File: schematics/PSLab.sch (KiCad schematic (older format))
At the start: 76 parts, among them J1 Programmer, J10 GND, J11 Vbus, J13 D+, J14 D-, J15 External Power, J16 I2C-2, J2 DoublePins, J5 Bluetooth, J6 I2C-1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

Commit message: docs: bill of materials
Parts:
- U15: footprint Connector_PinHeader_2.54mm:PinHeader_2x04_P2.54mm_Vertical -> Custom_Components:ESP-01
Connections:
- net +5V: now also J15.1 (Pin_1); no longer J7.1 (Pin_1)
- net ERxD: now also U15.2 (TX); no longer U15.1 (GND)
- net ETxD: now also U15.7 (RX); no longer U15.5 (IO0)
- net ExP: no longer J15.1 (Pin_1)
- net GND: now also U15.1 (GND); no longer U15.8 (VCC)
- net Vdd: now also U15.8 (VCC); no longer U15.2 (TX)
- net IOut: now reaches U3.38 (SCL1/RPI53/RC5)
- net IOut: now also J7.1 (Pin_1)
- no-connect marks 13 -> 12
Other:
- moved on the sheet: C2, R56, R57
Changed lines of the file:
@@
 	-1   0    0    1
 $EndComp
-Text Label 8395 1700 1    60   ~ 0
+Text Label 8910 1710 2    60   ~ 0
 Vdd
 $Comp
 L PSLab-rescue:GND-RESCUE-proto1 #PWR020
 U 1 1 55654875
-P 9170 1175
-F 0 "#PWR020" H 9170 1175 30  0001 C CNN
-F 1 "GND" H 9170 1105 30  0001 C CNN
-F 2 "" H 9170 1175 60  0000 C CNN
-F 3 "" H 9170 1175 60  0000 C CNN
-	1    9170 1175
-	0    -1   -1   0
+P 8470 1175
+F 0 "#PWR020" H 8470 1175 30  0001 C CNN
+F 1 "GND" H 8470 1105 30  0001 C CNN
+F 2 "" H 8470 1175 60  0000 C CNN
+F 3 "" H 8470 1175 60  0000 C CNN
+	1    8470 1175
+	0    1    1    0
 $EndComp
 $Comp
@@
 	0    1    1    0
 $EndComp
-Text Label 9345 1025 1    60   ~ 0
+Text Label 9330 1025 1    60   ~ 0
 ETxD
-Text Label 8395 825  3    60   ~ 0
+Text Label 8395 1040 3    60   ~ 0
 ERxD
 Text GLabel 6085 6665 0    40   Input ~ 0
@@
 L PSLab-rescue:R-RESCUE-proto1 R57
 U 1 1 56654C7F
-P 7775 850
-F 0 "R57" V 7855 850 40  0000 C CNN
-F 1 "18" V 7782 851 40  0000 C CNN
-F 2 "Resistor_SMD:R_0603_1608Metric" V 7705 850 30  0001 C CNN
-F 3 "" H 7775 850 30  0000 C CNN
-	1    7775 850
+P 7760 660
+F 0 "R57" V 7840 660 40  0000 C CNN
+F 1 "18" V 7767 661 40  0000 C CNN
+F 2 "Resistor_SMD:R_0603_1608Metric" V 7690 660 30  0001 C CNN
+F 3 "" H 7760 660 30  0000 C CNN
+	1    7760 660
 	0    1    -1   0
 $EndComp
@@
 L PSLab-rescue:R-RESCUE-proto1 R56
 U 1 1 5665622A
-P 7775 650
-F 0 "R56" V 7855 650 40  0000 C CNN
-F 1 "18" V 7782 651 40  0000 C CNN
-F 2 "Resistor_SMD:R_0603_1608Metric" V 7705 650 30  0001 C CNN
-F 3 "" H 7775 650 30  0000 C CNN
-	1    7775 650
+P 7760 880
+F 0 "R56" V 7840 880 40  0000 C CNN
+F 1 "18" V 7767 881 40  0000 C CNN
+F 2 "Resistor_SMD:R_0603_1608Metric" V 7690 880 30  0001 C CNN
+F 3 "" H 7760 880 30  0000 C CNN
+	1    7760 880
 	0    1    -1   0
 $EndComp
@@
 	-1   0    0    1
 $EndComp
-Text GLabel 7175 1895 1    40   Input ~ 0
-+5V
 Text GLabel 1415 3550 0    40   Input ~ 0
 SQR1
@@
 L PSLab-rescue:GND-RESCUE-proto1 #PWR046
 U 1 1 5564F446
-P 9220 1900
-F 0 "#PWR046" H 9220 1900 30  0001 C CNN
-F 1 "GND" H 9220 1830 30  0001 C CNN
-F 2 "" H 9220 1900 60  0000 C CNN
-F 3 "" H 9220 1900 60  0000 C CNN
-	1    9220 1900
+P 8225 2040
+F 0 "#PWR046" H 8225 2040 30  0001 C CNN
+F 1 "GND" H 8225 1970 30  0001 C CNN
+F 2 "" H 8225 2040 60  0000 C CNN
+F 3 "" H 8225 2040 60  0000 C CNN
+	1    8225 2040
 	1    0    0    -1
 $EndComp
@@
 L PSLab-rescue:C-RESCUE-proto1 C2
 U 1 1 5564F04A
-P 8820 1775
-F 0 "C2" H 8820 1875 40  0000 L CNN
-F 1 "0.1u" H 8826 1690 40  0000 L CNN
-F 2 "Capacitor_SMD:C_0603_1608Metric" H 8858 1625 30  0001 C CNN
-F 3 "" H 8820 1775 60  0000 C CNN
-	1    8820 1775
-	0    -1   -1   0
+P 8225 1840
+F 0 "C2" H 8225 1940 40  0000 L CNN
+F 1 "0.1u" H 8231 1755 40  0000 L CNN
+F 2 "Capacitor_SMD:C_0603_1608Metric" H 8263 1690 30  0001 C CNN
+F 3 "" H 8225 1840 60  0000 C CNN
+	1    8225 1840
+	1    0    0    -1
 $EndComp
 Text GLabel 5450 2300 1    47   Input ~ 0
@@
 Wire Wire Line
 	8195 5520 8370 5520
-Wire Wire Line
-	8200 750  9345 750
-Wire Wire Line
-	8200 750  8200 850
-Wire Wire Line
-	8200 850  8025 850
 Wire Notes Line
 	500  2750 4075 2750
@@
 F 0 "U15" H 9020 1625 39  0000 C CNN
 F 1 "ESP01" H 8670 1625 39  0000 C CNN
-F 2 "Connector_PinHeader_2.54mm:PinHeader_2x04_P2.54mm_Vertical" H 8820 1325 60  0001 C CNN
+F 2 "Custom_Components:ESP-01" H 8820 1325 60  0001 C CNN
 F 3 "" H 8820 1325 60  0001 C CNN
 	1    8820 1325
 	1    0    0    -1
 $EndComp
-Wire Wire Line
-	8470 1475 8395 1475
-Wire Wire Line
-	8470 1275 8395 1275
-Wire Wire Line
-	8395 1275 8395 1475
-Connection ~ 8395 1475
-NoConn ~ 9170 1275
-Wire Wire Line
-	8470 1175 8395 1175
-Wire Wire Line
-	8395 1175 8395 650
-Wire Wire Line
-	9170 1475 9345 1475
-Wire Wire Line
-	9345 1475 9345 750
-Wire Wire Line
-	9220 1900 9220 1775
-Wire Wire Line
-	9220 1775 9020 1775
-Wire Wire Line
-	8620 1775 8395 1775
-Wire Wire Line
-	8395 1475 8395 1775
 $Sheet
 S 1310 1190 550  305
@@
 	1    0    0    -1
 $EndComp
-Wire Wire Line
-	8395 650  8025 650
 Wire Notes Line
 	8040 550  8040 2175
@@
 Wire Notes Line
 	7750 2270 7750 4950
-Text GLabel 10100 1030 2    39   Input ~ 8
-ExP
 $Comp
 L Connector_Generic:Conn_01x05 J7
@@
 	0    1    1    0
 $EndComp
-NoConn ~ 5050 2600
 NoConn ~ 8470 1375
-NoConn ~ 9170 1375
 $Comp
 L PSLab-rescue:R-RESCUE-proto1 R55
@@
 RxD2
 Wire Wire Line
-	6975 650  7525 650
-Wire Wire Line
-	7075 1895 7075 850
-Wire Wire Line
-	7075 850  7525 850
-Wire Wire Line
-	6975 1895 6975 650
+	6975 1895 6975 880
+Wire Wire Line
+	8470 1275 8395 1275
+Wire Wire Line
+	9170 1275 9330 1275
+Wire Wire Line
+	9265 1175 9170 1175
+NoConn ~ 9170 1475
+NoConn ~ 9170 1375
+Wire Wire Line
+	7075 660  7510 660
+Wire Wire Line
+	7075 660  7075 1895
+Wire Wire Line
+	8010 660  9330 660
+Wire Wire Line
+	9330 660  9330 1275
+Wire Wire Line
+	7510 880  6975 880
+Wire Wire Line
+	8010 880  8395 880
+Wire Wire Line
+	8395 880  8395 1275
+Wire Wire Line
+	8225 1475 8395 1475
+Wire Wire Line
+	8395 1475 8395 1710
+Wire Wire Line
+	8395 1710 9265 1710
+Connection ~ 8395 1475
+Wire Wire Line
+	8395 1475 8470 1475
+Wire Wire Line
+	8225 1475 8225 1640
+Wire Wire Line
+	9265 1175 9265 1710
+Text GLabel 5050 2300 1    47   Input ~ 0
+IOut
+Wire Wire Line
+	5050 2300 5050 2600
+Text GLabel 7175 1895 1    47   Input ~ 0
+IOut
+Text GLabel 10100 1030 2    40   Input ~ 0
++5V
 $EndSCHEMATC

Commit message: fix: updated bom with correct footprints
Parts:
- F2: value 2016L100PR(1A) -> 1.5A; footprint Fuse:Fuse_1206_3216Metric -> Fuse:Fuse_1812_4532Metric
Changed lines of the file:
@@
 P 10690 930
 F 0 "F2" V 10517 930 39  0000 C CNN
-F 1 "2016L100PR(1A)" V 10592 930 39  0000 C CNN
-F 2 "Fuse:Fuse_1206_3216Metric" V 10620 930 50  0001 C CNN
-F 3 "https://www.mouser.se/datasheet/2/240/Littelfuse_PTC_2016L_Datasheet.pdf-1372437.pdf" H 10690 930 50  0001 C CNN
+F 1 "1.5A" V 10592 930 39  0000 C CNN
+F 2 "Fuse:Fuse_1812_4532Metric" V 10620 930 50  0001 C CNN
+F 3 "https://www.mouser.fi/datasheet/2/240/Littelfuse_PTC_1812L_Datasheet.pdf-693388.pdf" H 10690 930 50  0001 C CNN
 	1    10690 930
 	0    1    1    0

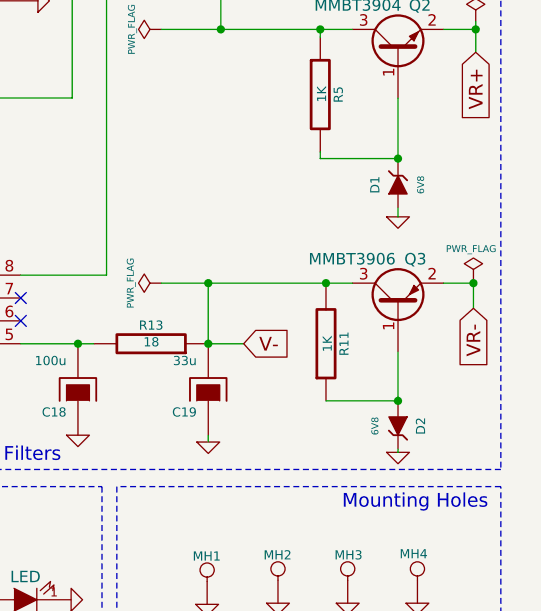
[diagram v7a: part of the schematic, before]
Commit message: fix: position correction for production
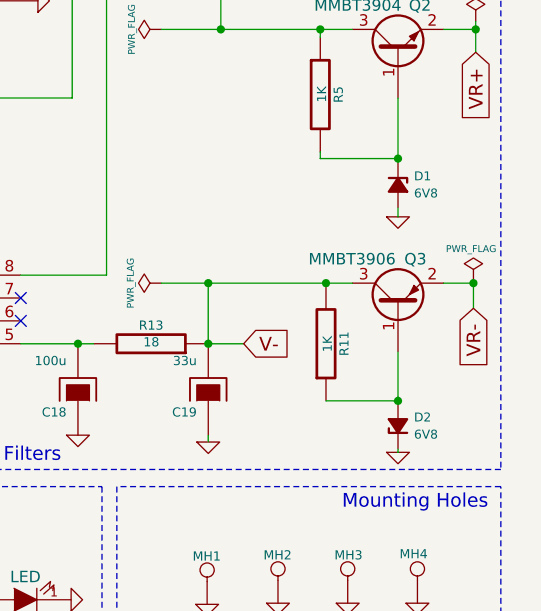
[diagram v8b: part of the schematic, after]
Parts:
- removed D1, D2: 6V8, Diode_SMD:D_MiniMELF, symbol PSLab-rescue:ZENERsmall-RESCUE-proto1
- added D1, D2: 6V8, Diode_SMD:D_MiniMELF, symbol Device:D_Zener_Small_ALT
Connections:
- net GND: now also D1.2 (A), D2.1 (K)
- net at Q2.1 (B), R5.2: now also D1.1 (K)
- net at Q3.1 (B), R11.1: now also D2.2 (A)
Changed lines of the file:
@@
-$EndComp
-$Comp
-L PSLab-rescue:ZENERsmall-RESCUE-proto1 D1
-U 1 1 55BABFCA
-P 10700 3705
-F 0 "D1" H 10700 3805 40  0000 C CNN
-F 1 "6V8" H 10700 3605 30  0000 C CNN
-F 2 "Diode_SMD:D_MiniMELF" H 10700 3705 60  0001 C CNN
-F 3 "" H 10700 3705 60  0000 C CNN
-	1    10700 3705
-	0    -1   -1   0
 $EndComp
 $Comp
@@
 	1    10700 3845
 	1    0    0    -1
-$EndComp
-$Comp
-L PSLab-rescue:ZENERsmall-RESCUE-proto1 D2
-U 1 1 55BACB8F
-P 10700 4760
-F 0 "D2" H 10700 4860 40  0000 C CNN
-F 1 "6V8" H 10700 4660 30  0000 C CNN
-F 2 "Diode_SMD:D_MiniMELF" H 10700 4760 60  0001 C CNN
-F 3 "" H 10700 4760 60  0000 C CNN
-	1    10700 4760
-	0    1    1    0
 $EndComp
 $Comp
@@
 	10385 4135 10385 4150
 Wire Wire Line
-	10700 4435 10700 4650
-Wire Wire Line
 	10700 4860 10700 4875
 Connection ~ 10385 4135
 Wire Wire Line
 	10385 4650 10700 4650
-Connection ~ 10700 4650
 Wire Wire Line
 	10700 3805 10700 3845
@@
 Text GLabel 10100 1030 2    40   Input ~ 0
 +5V
+$Comp
+L Device:D_Zener_Small_ALT D1
+U 1 1 5F52A60A
+P 10700 3705
+F 0 "D1" V 10662 3775 39  0000 L CNN
+F 1 "6V8" V 10737 3775 39  0000 L CNN
+F 2 "Diode_SMD:D_MiniMELF" V 10700 3705 50  0001 C CNN
+F 3 "~" V 10700 3705 50  0001 C CNN
+	1    10700 3705
+	0    1    1    0
+$EndComp
+$Comp
+L Device:D_Zener_Small_ALT D2
+U 1 1 5F551CE5
+P 10700 4760
+F 0 "D2" V 10738 4690 39  0000 R CNN
+F 1 "6V8" V 10663 4690 39  0000 R CNN
+F 2 "Diode_SMD:D_MiniMELF" V 10700 4760 50  0001 C CNN
+F 3 "~" V 10700 4760 50  0001 C CNN
+	1    10700 4760
+	0    -1   -1   0
+$EndComp
+Wire Wire Line
+	10700 4650 10700 4435
+Connection ~ 10700 4650
 $EndSCHEMATC
